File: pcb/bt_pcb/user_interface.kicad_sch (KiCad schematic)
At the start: 69 parts, among them J10 Conn_01x04, J11 Conn_01x04, J12 Conn_01x05, J7 Conn_01x04, J8 Conn_01x10, J9 Conn_01x04, SW1 SW_Push, SW10 SW_Push, SW2 SW_Push, SW3 SW_Push, SW4 SW_Push, SW5 SW_Push, SW6 SW_Push, SW7 SW_Push, SW8 SW_Push, SW9 SW_Push

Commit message: doing pcb from scratch again
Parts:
- removed J10, J11, J7, J9: Conn_01x04, Connector_PinHeader_2.54mm:PinHeader_1x04_P2.54mm_Vertical, symbol Connector_Generic:Conn_01x04
- removed J12: Conn_01x05, Connector_PinHeader_2.54mm:PinHeader_1x05_P2.54mm_Vertical, symbol Connector_Generic:Conn_01x05
- removed J8: Conn_01x10, Connector_PinHeader_2.54mm:PinHeader_1x10_P2.54mm_Vertical, symbol Connector_Generic:Conn_01x10
- removed R12, R14, R16, R18: 10k, Resistor_SMD:R_0603_1608Metric_Pad0.98x0.95mm_HandSolder, symbol Device:R
- added J10, J11, J6, J8: Conn_01x03, Connector_JST:JST_PH_B3B-PH-K_1x03_P2.00mm_Vertical, symbol Connector_Generic:Conn_01x03
- added J7: ER-OLEDM0383-1-SPI_Conn_01x10, library:ER-OLEDM0383-1-SPI, symbol Connector_Generic:Conn_01x10
- added SW1: RotaryEncoder_Switch, Rotary_Encoder:RotaryEncoder_Alps_EC11E-Switch_Vertical_H20mm_CircularMountingHoles, symbol Device:RotaryEncoder_Switch
- RV4: footprint Connector_PinHeader_2.54mm:PinHeader_1x03_P2.54mm_Vertical -> Potentiometer_THT:Potentiometer_Alpha_RD901F-40-00D_Single_Vertical_CircularHoles
- renumbered R13 to R10, R15 to R13, R17 to R14, R19 to R15, R20 to R16, R21 to R17, R22 to R18, R23 to R19, R24 to R20, R25 to R21, R26 to R22, R27 to R23, R28 to R24, R29 to R25, R30 to R26, R31 to R27, R32 to R28, R33 to R29, R34 to R30, R35 to R31, R36 to R32, R37 to R33, R38 to R34, R11 to R7, SW9 to SW10, SW10 to SW11, SW1 to SW2, SW2 to SW3, SW3 to SW4, SW4 to SW5, SW5 to SW6, SW6 to SW7, SW7 to SW8, SW8 to SW9
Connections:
- net +3V3: now also J10.3 (Pin_3), J11.3 (Pin_3), J6.3 (Pin_3), J7.2 (Pin_2), J8.3 (Pin_3), SW1.S1
- net DISPLAY_GPIO_0: now also J7.6 (Pin_6)
- net DISPLAY_GPIO_1: now also J7.7 (Pin_7)
- net DISPLAY_GPIO_2: now also J7.8 (Pin_8)
- net DISPLAY_GPIO_3: now also J7.9 (Pin_9)
- net DISPLAY_GPIO_4: now also J7.10 (Pin_10)
- net DISPLAY_SPI_MISO: now also J7.5 (Pin_5)
- net DISPLAY_SPI_MOSI: now also J7.4 (Pin_4)
- net DISPLAY_SPI_SCK: now also J7.3 (Pin_3)
- net ENC_A: now also SW1.A
- net ENC_B: now also SW1.B
- net ENC_SW: now also SW1.S2
- net EXP_0: now also J6.2 (Pin_2)
- net EXP_1: now also J8.2 (Pin_2)
- net EXP_2: now also J10.2 (Pin_2)
- net EXP_3: now also J11.2 (Pin_2)
- net GND: now also J10.1 (Pin_1), J11.1 (Pin_1), J6.1 (Pin_1), J7.1 (Pin_1), J8.1 (Pin_1), SW1.C
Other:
- note added: "T --> 3 R --> 2 TN, RN, SN, S --> 1"
- note removed: "T --> 4 R --> 3 SN --> 2 TN, RN, S --> 1"
- moved on the sheet: C34, R17

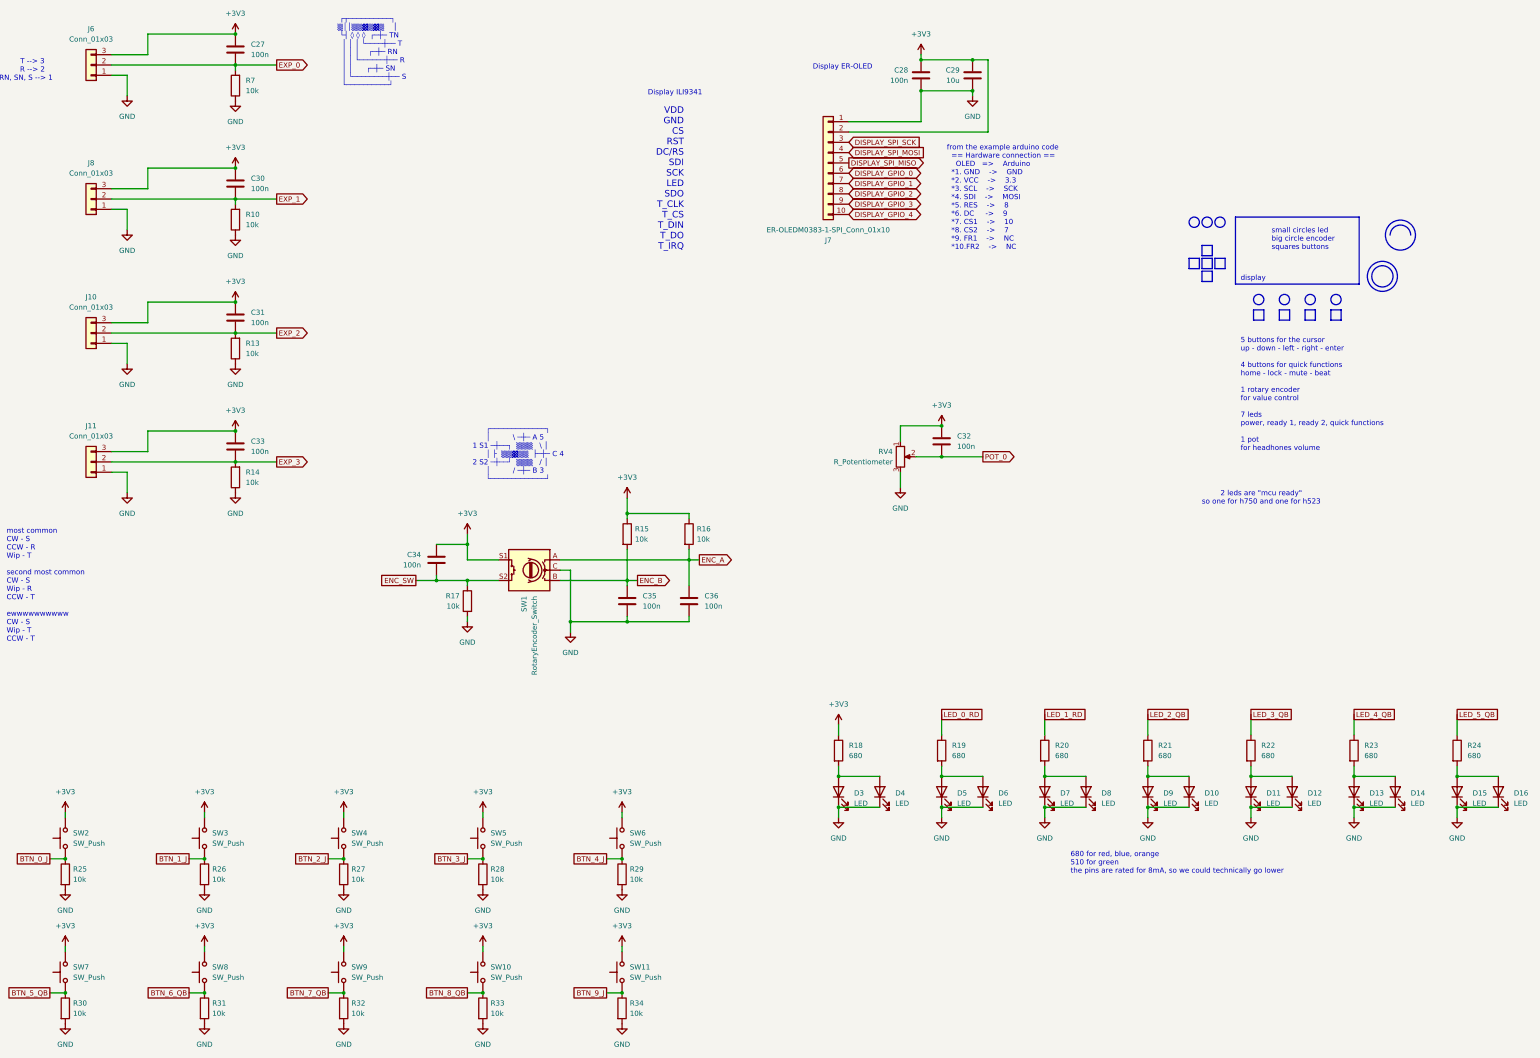
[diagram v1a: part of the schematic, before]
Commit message: redo of power supply
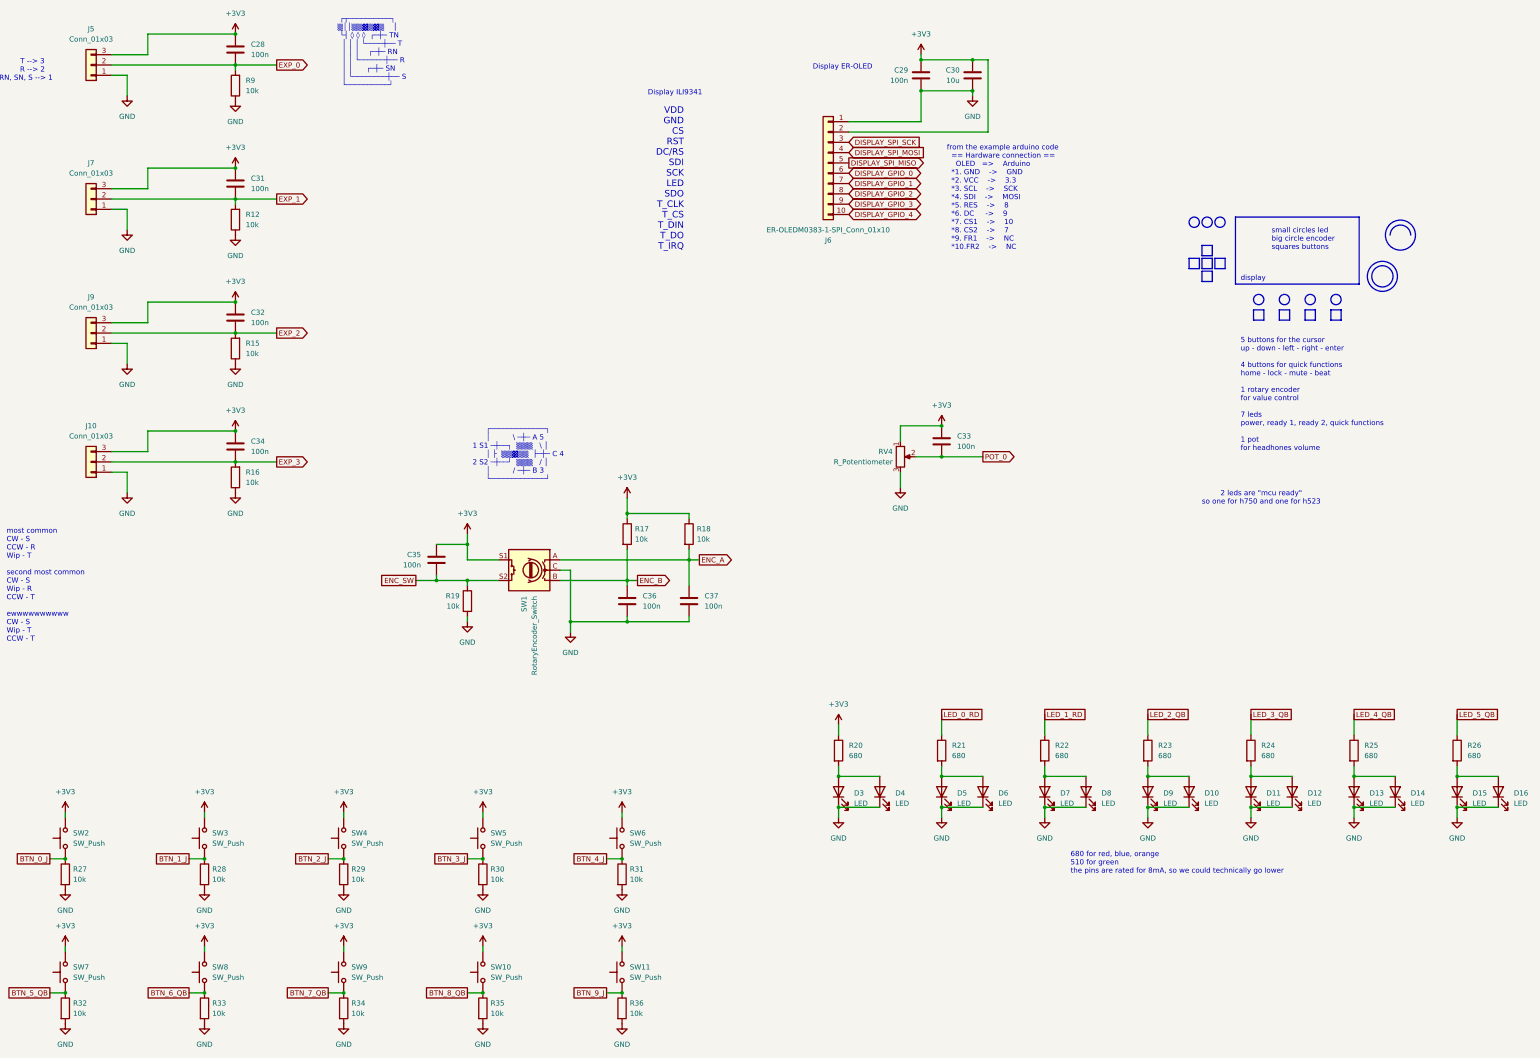
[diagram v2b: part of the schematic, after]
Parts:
- renumbered C27 to C28, C28 to C29, C29 to C30, C30 to C31, C31 to C32, C32 to C33, C33 to C34, C34 to C35, C35 to C36, C36 to C37, J11 to J10, J6 to J5, J7 to J6, J8 to J7, J10 to J9, R10 to R12, R13 to R15, R14 to R16, R15 to R17, R16 to R18, R17 to R19, R18 to R20, R19 to R21, R20 to R22, R21 to R23, R22 to R24, R23 to R25, R24 to R26, R25 to R27, R26 to R28, R27 to R29, R28 to R30, R29 to R31, R30 to R32, R31 to R33, R32 to R34, R33 to R35, R34 to R36, R7 to R9

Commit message: made a bom
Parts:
- J10, J5, J6, J7, J9: now left out of the parts list

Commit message: seeing the end of the tunnel
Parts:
- added J10: Conn_01x03, Connector_JST:JST_PH_B3B-PH-K_1x03_P2.00mm_Vertical, symbol Connector_Generic:Conn_01x03
- R20, R21, R22, R23, R24, R25, R26: value 680 -> 680/510
- renumbered J10 to J11
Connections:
- net +3V3: now also J10.3 (Pin_3)
- net GND: now also J10.1 (Pin_1)
- net POT_0: now also J10.2 (Pin_2)

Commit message: aaaaaaa
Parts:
- renumbered C28 to C35, C31 to C36, C32 to C37, C34 to C38, C35 to C39, C36 to C40, C37 to C41, C29 to C42, C33 to C43, C30 to C44, J5 to J3, J7 to J4, J9 to J5, J11 to J6, J10 to J8, J6 to J9, R9 to R10, R12 to R11, R15 to R12, R16 to R13, R29 to R14, R34 to R15, R19 to R18, R30 to R19, R35 to R20, R31 to R21, R36 to R22, R17 to R23, R18 to R24, R20 to R25, R21 to R28, R22 to R29, R23 to R30, R24 to R31, R25 to R32, R26 to R33, R27 to R6, R32 to R7, R28 to R8, R33 to R9, SW2 to SW1, SW6 to SW10, SW7 to SW2, SW8 to SW4, SW4 to SW5, SW9 to SW6, SW5 to SW7, SW10 to SW8, SW1 to SW9

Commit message: schematic rev b finish?
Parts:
- renumbered C35 to C50, C42 to C51, C44 to C52, C36 to C53, C37 to C54, C43 to C55, C38 to C56, C39 to C57, C40 to C58, C41 to C59, J6 to J10, J3 to J4, J9 to J5, J4 to J6, J5 to J8, J8 to J9, R11 to R12, R12 to R13, R13 to R14, R23 to R15, R24 to R16, R18 to R17, R25 to R18, R28 to R19, R29 to R20, R30 to R21, R31 to R22, R32 to R23, R33 to R24, R6 to R25, R8 to R26, R14 to R27, R19 to R28, R21 to R29, R7 to R30, R9 to R31, R15 to R32, R20 to R33, R22 to R34, R10 to R7, SW9 to SW1, SW8 to SW10, SW1 to SW2, SW5 to SW4, SW7 to SW5, SW10 to SW6, SW2 to SW7, SW4 to SW8, SW6 to SW9

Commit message: sd kind of in
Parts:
- renumbered R13 to R10, R14 to R11, R15 to R12, R16 to R13, R17 to R14, R18 to R15, R19 to R16, R20 to R17, R21 to R18, R22 to R19, R23 to R20, R24 to R21, R25 to R22, R26 to R23, R27 to R24, R28 to R25, R29 to R26, R30 to R27, R31 to R28, R32 to R29, R33 to R30, R34 to R31, R7 to R4, R12 to R9
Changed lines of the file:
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@@
 		(dnp no)
 		(fields_autoplaced yes)
-		(property "Reference" "R17"
+		(property "Reference" "R14"
 			(at 135.255 162.56 0)
 			(show_name no)
@@
 			(project "bt_pcb"
 				(path "/eb787481-08cd-41a4-a128-173fa6227c32/4fcd5c8c-58b7-4ce7-9521-e6e7fa7f5f34"
-					(reference "R17")
+					(reference "R14")
 					(unit 1)
 				)
@@
 		(dnp no)
 		(fields_autoplaced yes)
-		(property "Reference" "R31"
+		(property "Reference" "R28"
 			(at 74.295 262.89 0)
 			(show_name no)
@@
 			(project "bt_pcb"
 				(path "/eb787481-08cd-41a4-a128-173fa6227c32/4fcd5c8c-58b7-4ce7-9521-e6e7fa7f5f34"
-					(reference "R31")
+					(reference "R28")
 					(unit 1)
 				)
@@
 		(dnp no)
 		(fields_autoplaced yes)
-		(property "Reference" "R26"
+		(property "Reference" "R23"
 			(at 74.295 229.87 0)
 			(show_name no)
@@
 			(project "bt_pcb"
 				(path "/eb787481-08cd-41a4-a128-173fa6227c32/4fcd5c8c-58b7-4ce7-9521-e6e7fa7f5f34"
-					(reference "R26")
+					(reference "R23")
 					(unit 1)
 				)
@@
 		(dnp no)
 		(fields_autoplaced yes)
-		(property "Reference" "R7"
+		(property "Reference" "R4"
 			(at 82.55 35.56 0)
 			(show_name no)
@@
 			(project "bt_pcb"
 				(path "/eb787481-08cd-41a4-a128-173fa6227c32/4fcd5c8c-58b7-4ce7-9521-e6e7fa7f5f34"
-					(reference "R7")
+					(reference "R4")
 					(unit 1)
 				)
@@
 		(dnp no)
 		(fields_autoplaced yes)
-		(property "Reference" "R20"
+		(property "Reference" "R17"
 			(at 281.94 199.3899 0)
 			(show_name no)
@@
 			(project "bt_pcb"
 				(path "/eb787481-08cd-41a4-a128-173fa6227c32/4fcd5c8c-58b7-4ce7-9521-e6e7fa7f5f34"
-					(reference "R20")
+					(reference "R17")
 					(unit 1)
 				)
@@
 		(dnp no)
 		(fields_autoplaced yes)
-		(property "Reference" "R28"
+		(property "Reference" "R25"
 			(at 142.875 229.87 0)
 			(show_name no)
@@
 			(project "bt_pcb"
 				(path "/eb787481-08cd-41a4-a128-173fa6227c32/4fcd5c8c-58b7-4ce7-9521-e6e7fa7f5f34"
-					(reference "R28")
+					(reference "R25")
 					(unit 1)
 				)
@@
 		(dnp no)
 		(fields_autoplaced yes)
-		(property "Reference" "R30"
+		(property "Reference" "R27"
 			(at 40.005 262.89 0)
 			(show_name no)
@@
 			(project "bt_pcb"
 				(path "/eb787481-08cd-41a4-a128-173fa6227c32/4fcd5c8c-58b7-4ce7-9521-e6e7fa7f5f34"
-					(reference "R30")
+					(reference "R27")
 					(unit 1)
 				)
@@
 		(dnp no)
 		(fields_autoplaced yes)
-		(property "Reference" "R21"
+		(property "Reference" "R18"
 			(at 307.34 199.3899 0)
 			(show_name no)
@@
 			(project "bt_pcb"
 				(path "/eb787481-08cd-41a4-a128-173fa6227c32/4fcd5c8c-58b7-4ce7-9521-e6e7fa7f5f34"
-					(reference "R21")
+					(reference "R18")
 					(unit 1)
 				)
@@
 		(dnp no)
 		(fields_autoplaced yes)
-		(property "Reference" "R24"
+		(property "Reference" "R21"
 			(at 383.54 199.3899 0)
 			(show_name no)
@@
 			(project "bt_pcb"
 				(path "/eb787481-08cd-41a4-a128-173fa6227c32/4fcd5c8c-58b7-4ce7-9521-e6e7fa7f5f34"
-					(reference "R24")
+					(reference "R21")
 					(unit 1)
 				)
@@
 		(dnp no)
 		(fields_autoplaced yes)
-		(property "Reference" "R33"
+		(property "Reference" "R30"
 			(at 142.875 262.89 0)
 			(show_name no)
@@
 			(project "bt_pcb"
 				(path "/eb787481-08cd-41a4-a128-173fa6227c32/4fcd5c8c-58b7-4ce7-9521-e6e7fa7f5f34"
-					(reference "R33")
+					(reference "R30")
 					(unit 1)
 				)
@@
 		(in_pos_files yes)
 		(dnp no)
-		(property "Reference" "R15"
+		(property "Reference" "R12"
 			(at 178.435 146.05 0)
 			(show_name no)
@@
 			(project "bt_pcb"
 				(path "/eb787481-08cd-41a4-a128-173fa6227c32/4fcd5c8c-58b7-4ce7-9521-e6e7fa7f5f34"
-					(reference "R15")
+					(reference "R12")
 					(unit 1)
 				)
@@
 		(dnp no)
 		(fields_autoplaced yes)
-		(property "Reference" "R29"
+		(property "Reference" "R26"
 			(at 177.165 229.87 0)
 			(show_name no)
@@
 			(project "bt_pcb"
 				(path "/eb787481-08cd-41a4-a128-173fa6227c32/4fcd5c8c-58b7-4ce7-9521-e6e7fa7f5f34"
-					(reference "R29")
+					(reference "R26")
 					(unit 1)
 				)
@@
 		(dnp no)
 		(fields_autoplaced yes)
-		(property "Reference" "R18"
+		(property "Reference" "R15"
 			(at 231.14 199.39 0)
 			(show_name no)
@@
 			(project "bt_pcb"
 				(path "/eb787481-08cd-41a4-a128-173fa6227c32/4fcd5c8c-58b7-4ce7-9521-e6e7fa7f5f34"
-					(reference "R18")
+					(reference "R15")
 					(unit 1)
 				)
@@
 		(dnp no)
 		(fields_autoplaced yes)
-		(property "Reference" "R14"
+		(property "Reference" "R11"
 			(at 82.55 132.08 0)
 			(show_name no)
@@
 			(project "bt_pcb"
 				(path "/eb787481-08cd-41a4-a128-173fa6227c32/4fcd5c8c-58b7-4ce7-9521-e6e7fa7f5f34"
-					(reference "R14")
+					(reference "R11")
 					(unit 1)
 				)
@@
 		(dnp no)
 		(fields_autoplaced yes)
-		(property "Reference" "R13"
+		(property "Reference" "R10"
 			(at 82.55 100.33 0)
 			(show_name no)
@@
 			(project "bt_pcb"
 				(path "/eb787481-08cd-41a4-a128-173fa6227c32/4fcd5c8c-58b7-4ce7-9521-e6e7fa7f5f34"
-					(reference "R13")
+					(reference "R10")
 					(unit 1)
 				)
@@
 		(dnp no)
 		(fields_autoplaced yes)
-		(property "Reference" "R23"
+		(property "Reference" "R20"
 			(at 358.14 199.3899 0)
 			(show_name no)
@@
 			(project "bt_pcb"
 				(path "/eb787481-08cd-41a4-a128-173fa6227c32/4fcd5c8c-58b7-4ce7-9521-e6e7fa7f5f34"
-					(reference "R23")
+					(reference "R20")
 					(unit 1)
 				)
@@
 		(dnp no)
 		(fields_autoplaced yes)
-		(property "Reference" "R22"
+		(property "Reference" "R19"
 			(at 332.74 199.3899 0)
 			(show_name no)
@@
 			(project "bt_pcb"
 				(path "/eb787481-08cd-41a4-a128-173fa6227c32/4fcd5c8c-58b7-4ce7-9521-e6e7fa7f5f34"
-					(reference "R22")
+					(reference "R19")
 					(unit 1)
 				)
@@
 		(dnp no)
 		(fields_autoplaced yes)
-		(property "Reference" "R34"
+		(property "Reference" "R31"
 			(at 177.165 262.89 0)
 			(show_name no)
@@
 			(project "bt_pcb"
 				(path "/eb787481-08cd-41a4-a128-173fa6227c32/4fcd5c8c-58b7-4ce7-9521-e6e7fa7f5f34"
-					(reference "R34")
+					(reference "R31")
 					(unit 1)
 				)
@@
 		(dnp no)
 		(fields_autoplaced yes)
-		(property "Reference" "R19"
+		(property "Reference" "R16"
 			(at 256.54 199.3899 0)
 			(show_name no)
@@
 			(project "bt_pcb"
 				(path "/eb787481-08cd-41a4-a128-173fa6227c32/4fcd5c8c-58b7-4ce7-9521-e6e7fa7f5f34"
-					(reference "R19")
+					(reference "R16")
 					(unit 1)
 				)
@@
 		(dnp no)
 		(fields_autoplaced yes)
-		(property "Reference" "R32"
+		(property "Reference" "R29"
 			(at 108.585 262.89 0)
 			(show_name no)
@@
 			(project "bt_pcb"
 				(path "/eb787481-08cd-41a4-a128-173fa6227c32/4fcd5c8c-58b7-4ce7-9521-e6e7fa7f5f34"
-					(reference "R32")
+					(reference "R29")
 					(unit 1)
 				)
@@
 		(dnp no)
 		(fields_autoplaced yes)
-		(property "Reference" "R12"
+		(property "Reference" "R9"
 			(at 82.55 68.58 0)
 			(show_name no)
@@
 			(project "bt_pcb"
 				(path "/eb787481-08cd-41a4-a128-173fa6227c32/4fcd5c8c-58b7-4ce7-9521-e6e7fa7f5f34"
-					(reference "R12")
+					(reference "R9")
 					(unit 1)
 				)
@@
 		(in_pos_files yes)
 		(dnp no)
-		(property "Reference" "R16"
+		(property "Reference" "R13"
 			(at 193.675 146.05 0)
 			(show_name no)
@@
 			(project "bt_pcb"
 				(path "/eb787481-08cd-41a4-a128-173fa6227c32/4fcd5c8c-58b7-4ce7-9521-e6e7fa7f5f34"
-					(reference "R16")
+					(reference "R13")
 					(unit 1)
 				)
@@
 		(dnp no)
 		(fields_autoplaced yes)
-		(property "Reference" "R25"
+		(property "Reference" "R22"
 			(at 40.005 229.87 0)
 			(show_name no)
@@
 			(project "bt_pcb"
 				(path "/eb787481-08cd-41a4-a128-173fa6227c32/4fcd5c8c-58b7-4ce7-9521-e6e7fa7f5f34"
-					(reference "R25")
+					(reference "R22")
 					(unit 1)
 				)
@@
 		(dnp no)
 		(fields_autoplaced yes)
-		(property "Reference" "R27"
+		(property "Reference" "R24"
 			(at 108.585 229.87 0)
 			(show_name no)
@@
 			(project "bt_pcb"
 				(path "/eb787481-08cd-41a4-a128-173fa6227c32/4fcd5c8c-58b7-4ce7-9521-e6e7fa7f5f34"
-					(reference "R27")
+					(reference "R24")
 					(unit 1)
 				)

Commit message: reb b finished
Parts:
- renumbered C50 to C43, C51 to C44, C52 to C45, C53 to C46, C54 to C47, C55 to C48, C56 to C49, C57 to C50, C58 to C51, C59 to C52, R9 to R11, R10 to R12, R11 to R13, R12 to R14, R13 to R15, R14 to R16, R15 to R17, R16 to R18, R17 to R19, R18 to R20, R19 to R21, R20 to R22, R21 to R23, R22 to R24, R23 to R25, R24 to R26, R25 to R27, R26 to R28, R27 to R29, R28 to R30, R29 to R31, R30 to R32, R31 to R33, R4 to R6
